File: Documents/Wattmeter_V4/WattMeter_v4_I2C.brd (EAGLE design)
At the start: 64.5 x 35.5 mm, 85 parts, among them Q1 QUARTZ_3.58M_2PIN, U1 ADE7953, U10 PS2505, U11 SN74LVC1G3157DBVR, U12 PS2505, U13 SN74LVC, U2 PAM2305, U3 ISO7241, U4 SN74LVC, U5 NL17SZ125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

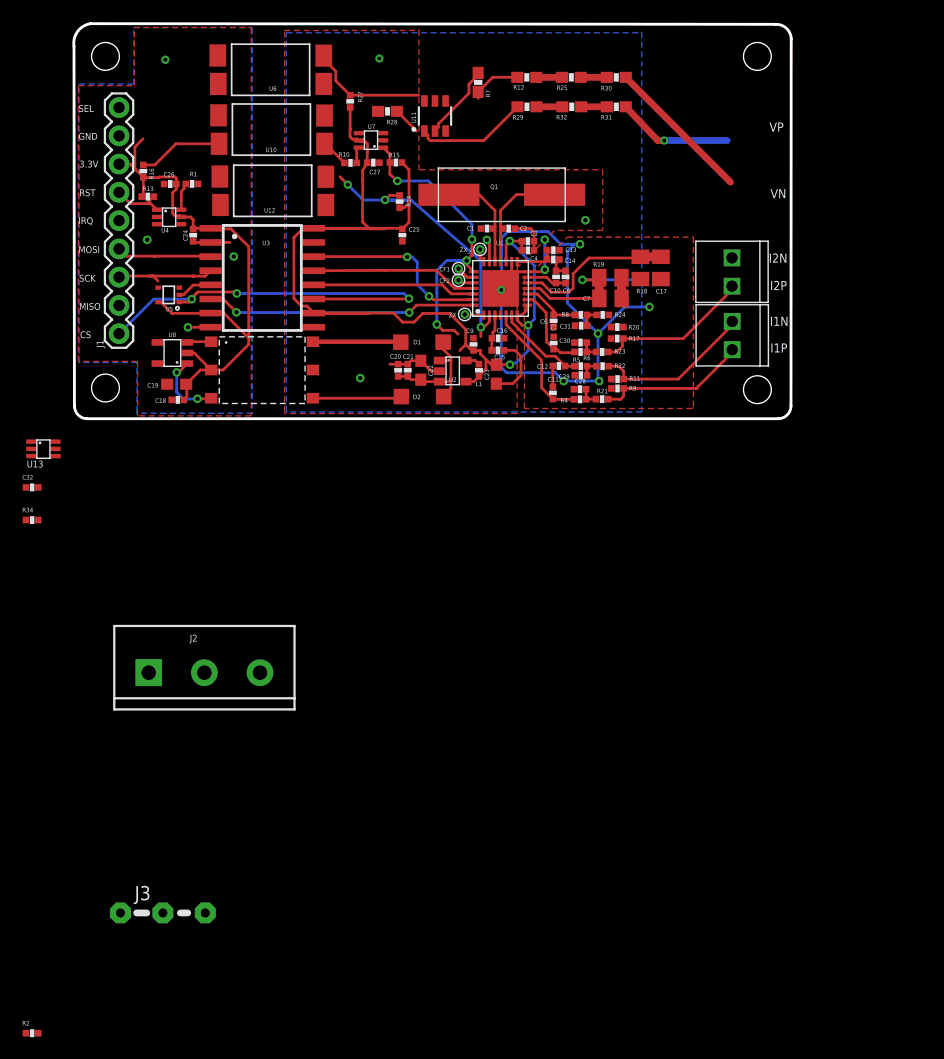
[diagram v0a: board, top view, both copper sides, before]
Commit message: latest updates for I2C and SPI
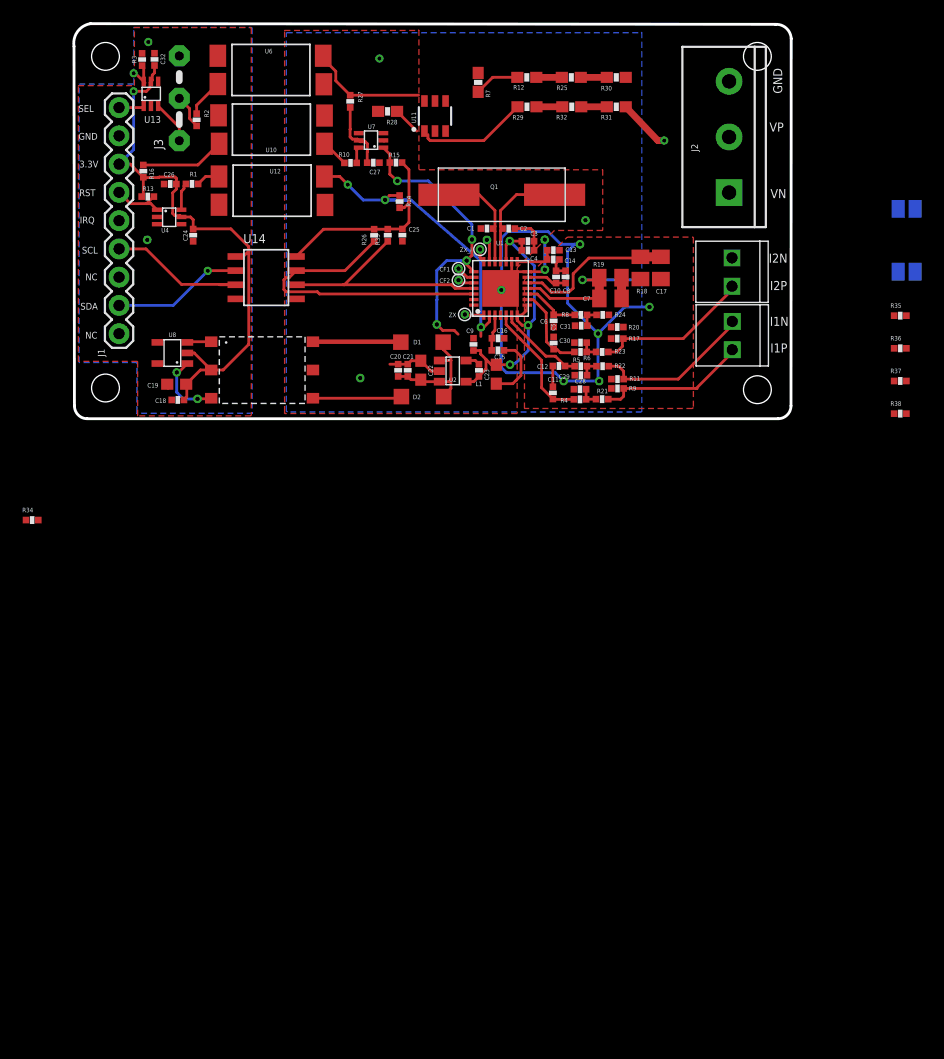
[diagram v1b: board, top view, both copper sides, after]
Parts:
- removed U3: ISO7241, Damien_divers:16-SOIC
- removed U5: NL17SZ125, wattmeter:NL17SZ125
- added R26, R3, R33, R35, R36: 4.7k, Nizanlib:0402-RES
- added R37, R38: 4.7K, Nizanlib:0402-RES
- added SJ1, SJ2: (no value), jumper:SJ
- added U14: ISO1541, wattmeter:ISO1541
- moved R2 83.4 mm to (11.3, 27.2), turned to 270 degrees
- moved J3 71.4 mm to (9.75, 27.2), turned to 90 degrees
- moved J2 67.7 mm to (59.2, 20.7), turned to 90 degrees
- moved C32 40.0 mm to (7.53, 32.6), turned to 90 degrees
- moved U13 33.5 mm to (7.85, 28.4), turned to 90 degrees
- moved U12 11.3 mm to (12.9, 18.5), turned to 0 degrees
- moved U6 11.3 mm to (12.8, 29.4), turned to 0 degrees
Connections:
- removed net CS: J1.1, U3.11, U5.1
- removed net MISO: U3.5, U5.2
- removed net MISO_ISO: U1.26, U3.12
- removed net MISO_OUT: J1.2, U5.4
- removed net MOSI: J1.4, U3.3
- removed net MOSI_ISO: U1.27, U3.14
- removed net SCK: J1.3, U3.4
- removed net SCK_ISO: U1.25, U3.13
- new net N$17: J3.3, U13.4
- new net N$29: R36.1, SJ1.1
- new net N$44: R35.1, SJ2.1
- new net SCL: J1.4, SJ2.2, U14.3
- new net SCLK_ISO: R38.1
- new net SCL_ISO: R33.1, U1.25, U1.27, U14.6
- new net SDA: J1.2, SJ1.2, U14.2
- new net SDA_ISO: R26.1, U1.26, U14.7
- net AGND: now also J2.3; no longer J2.1
- net CS_ISO: now also R37.1; no longer U3.6
- net GND: now also R3.1, U14.4; no longer U3.2, U3.8, U5.3
- net GNDI: now also U14.5; no longer U3.15, U3.9
- net LNV1: now also J2.1; no longer J2.2
- net LNV2: now also J2.2; no longer J2.3
- net N$40: now also R3.2, U13.3
- net SELECT: no longer J3.3
- net VCC: now also R26.2, R33.2, R37.2, R38.2, U14.8; no longer U3.10, U3.16
- net VDD: now also R35.2, R36.2, U14.1; no longer U3.1, U3.7, U5.5
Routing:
- net VCC: track 96.3 -> 52.1 mm
- net CS: track 37.7 -> 0.00 mm, vias 3 -> 0
- net SDA_ISO: track 0.00 -> 27.6 mm
- net CS_ISO: track 24.4 -> 0.00 mm, vias 2 -> 0
- net SCL_ISO: track 0.00 -> 21.6 mm
- net MOSI_ISO: track 17.2 -> 0.00 mm, vias 2 -> 0
- net MISO_ISO: track 15.1 -> 0.00 mm
- net SCK_ISO: track 15.0 -> 0.00 mm
- net LNV1: track 13.3 -> 0.00 mm
- net SCL: track 0.00 -> 13.3 mm
- net SDA: track 0.00 -> 11.8 mm, vias 0 -> 1
- net SCK: track 9.57 -> 0.00 mm
- net MOSI: track 8.68 -> 0.00 mm
- net N$40: track 0.00 -> 6.78 mm, vias 0 -> 1
- net AGND: track 63.8 -> 57.6 mm
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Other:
- board text added: "NC"
- board text added: "SCL"
- board text added: "SDA"
- board text removed: "CS"
- board text removed: "MISO"
- board text removed: "MOSI"
- board text removed: "SCK"
